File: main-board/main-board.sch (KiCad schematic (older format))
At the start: 112 parts, among them J1 BOOT, J10 8P8CDouble, J11 Qwiic, J12 Qwiic, J13 Qwiic, J14 YELLOW, J15 GREEN, J2 USB Header, J3 JTAG, J5 StatusPanel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

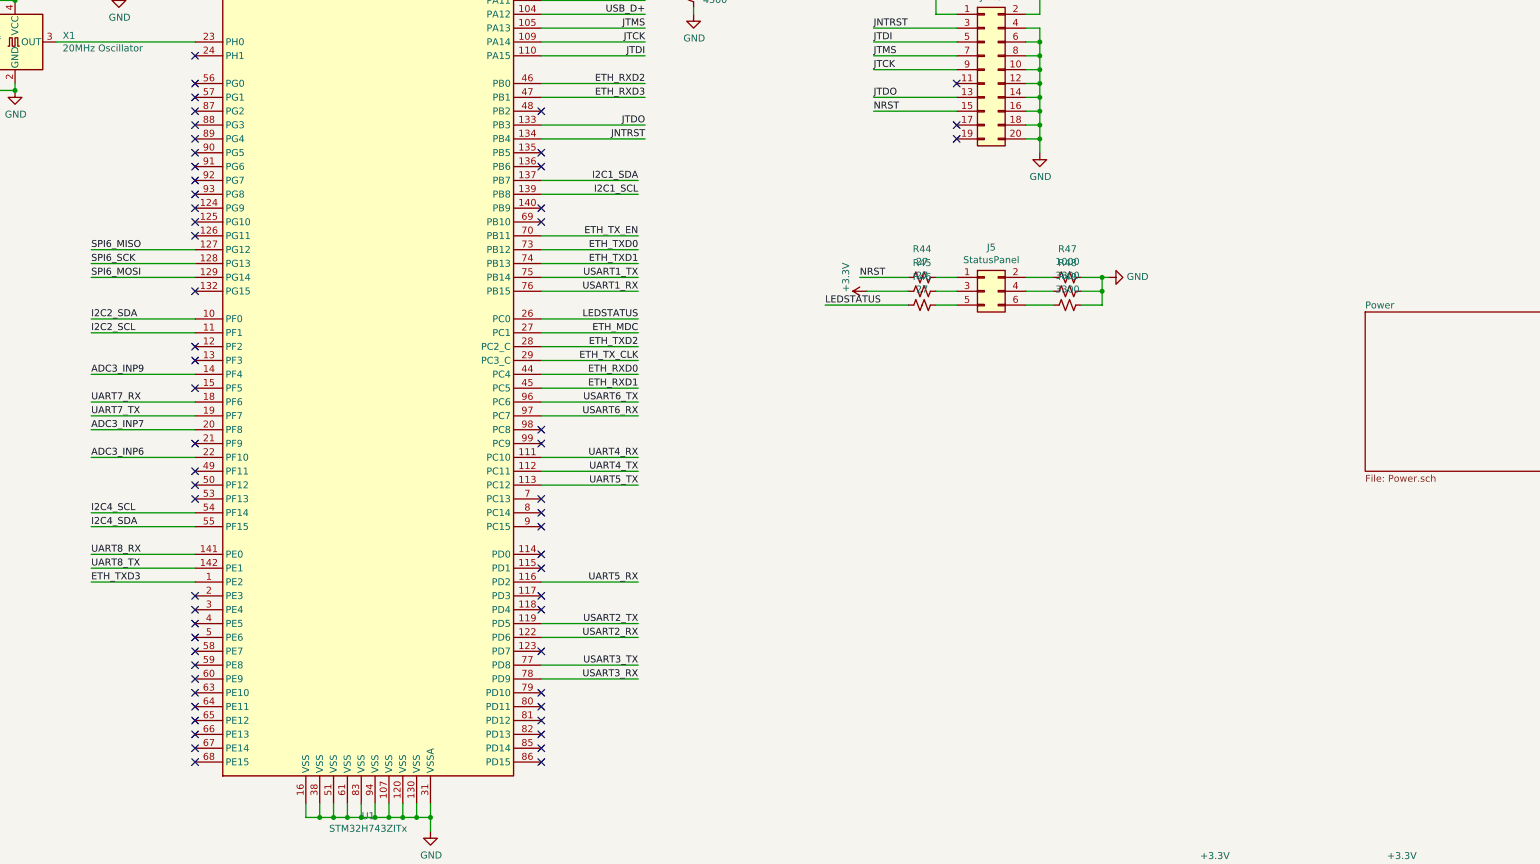
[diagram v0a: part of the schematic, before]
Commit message: GPIO control lines for the MOSFET array
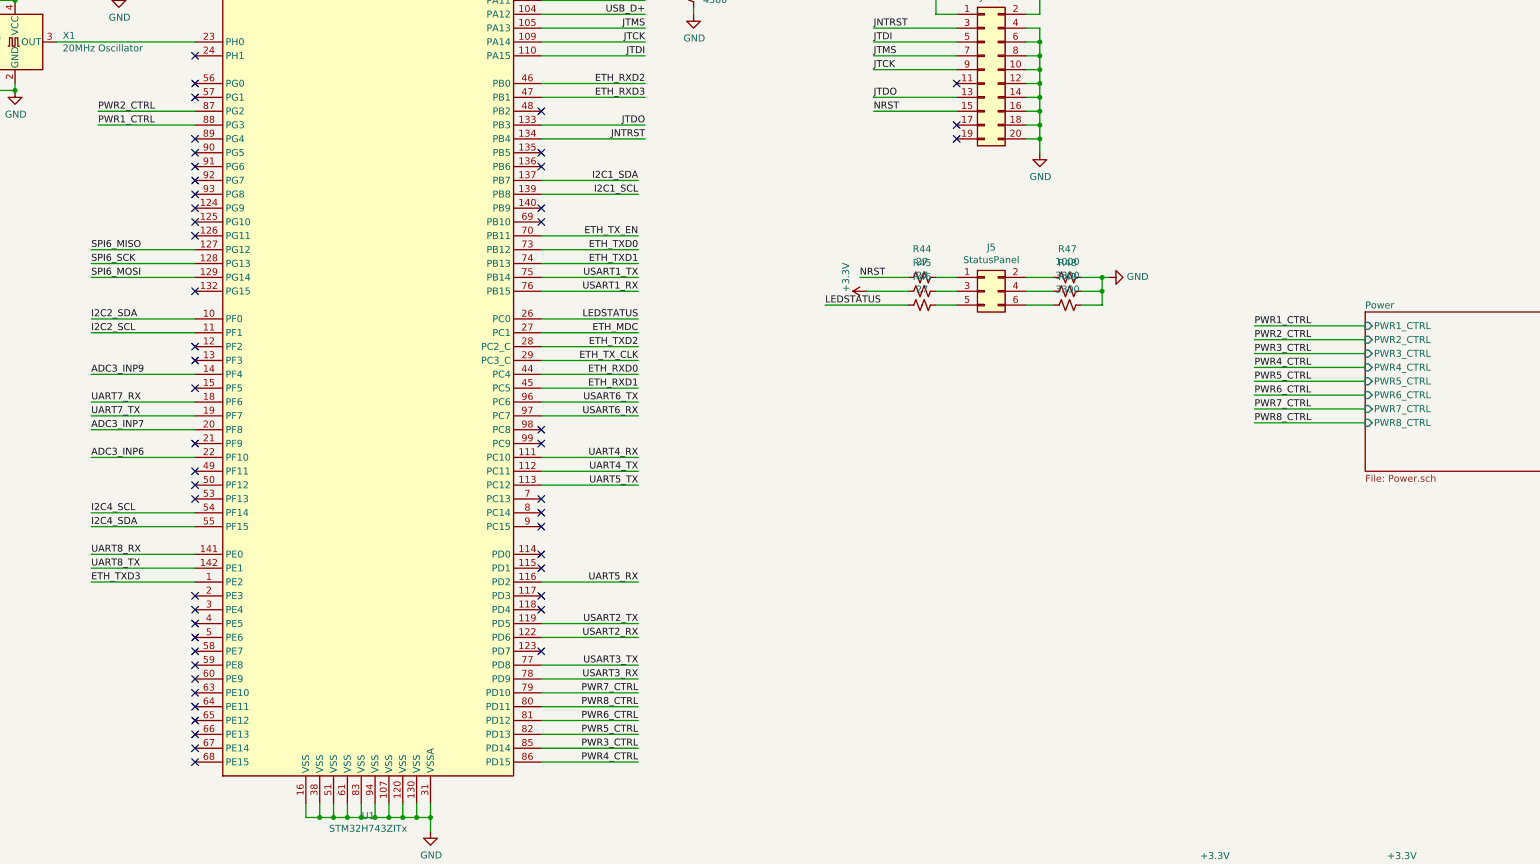
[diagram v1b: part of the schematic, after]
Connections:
- net PWR7_CTRL: now reaches U1.79 (PD10)
- net PWR8_CTRL: now reaches U1.80 (PD11)
- net PWR6_CTRL: now reaches U1.81 (PD12)
- net PWR5_CTRL: now reaches U1.82 (PD13)
- net PWR3_CTRL: now reaches U1.85 (PD14)
- net PWR4_CTRL: now reaches U1.86 (PD15)
- net PWR2_CTRL: now reaches U1.87 (PG2)
- net PWR1_CTRL: now reaches U1.88 (PG3)
- no-connect marks 66 -> 58
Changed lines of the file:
@@
 	2300 9450 2500 9450
 NoConn ~ 2500 9350
-NoConn ~ 13150 9700
-NoConn ~ 13150 9600
-NoConn ~ 13150 9500
-NoConn ~ 13150 9400
-NoConn ~ 13150 9300
-NoConn ~ 13150 9200
 NoConn ~ 13150 8900
 NoConn ~ 13150 7800
@@
 NoConn ~ 10650 5300
 NoConn ~ 10650 5200
-NoConn ~ 10650 5100
 NoConn ~ 10650 4800
 NoConn ~ 10650 4900
-NoConn ~ 10650 5000
 NoConn ~ 13150 3500
 NoConn ~ 13150 4100
@@
 F0 "Power" 50
 F1 "Power.sch" 50
+F2 "PWR1_CTRL" I L 19100 6550 50
+F3 "PWR3_CTRL" I L 19100 6750 50
+F4 "PWR2_CTRL" I L 19100 6650 50
+F5 "PWR4_CTRL" I L 19100 6850 50
+F6 "PWR6_CTRL" I L 19100 7050 50
+F7 "PWR5_CTRL" I L 19100 6950 50
+F8 "PWR7_CTRL" I L 19100 7150 50
+F9 "PWR8_CTRL" I L 19100 7250 50
 $EndSheet
 Connection ~ 9800 11250
@@
 Wire Wire Line
 	1050 2500 1300 2500
+Wire Wire Line
+	13150 9200 13850 9200
+Wire Wire Line
+	13150 9300 13850 9300
+Wire Wire Line
+	13150 9400 13850 9400
+Wire Wire Line
+	13150 9500 13850 9500
+Wire Wire Line
+	13150 9600 13850 9600
+Wire Wire Line
+	13150 9700 13850 9700
+Wire Wire Line
+	10650 5000 9950 5000
+Wire Wire Line
+	10650 5100 9950 5100
+Text Label 9950 5000 0    50   ~ 0
+PWR2_CTRL
+Text Label 9950 5100 0    50   ~ 0
+PWR1_CTRL
+Wire Wire Line
+	19100 6550 18300 6550
+Wire Wire Line
+	19100 6650 18300 6650
+Wire Wire Line
+	19100 6750 18300 6750
+Wire Wire Line
+	19100 6850 18300 6850
+Wire Wire Line
+	19100 6950 18300 6950
+Wire Wire Line
+	19100 7050 18300 7050
+Wire Wire Line
+	19100 7150 18300 7150
+Wire Wire Line
+	19100 7250 18300 7250
+Text Label 18300 6550 0    50   ~ 0
+PWR1_CTRL
+Text Label 18300 6650 0    50   ~ 0
+PWR2_CTRL
+Text Label 18300 6750 0    50   ~ 0
+PWR3_CTRL
+Text Label 18300 6850 0    50   ~ 0
+PWR4_CTRL
+Text Label 18300 6950 0    50   ~ 0
+PWR5_CTRL
+Text Label 18300 7050 0    50   ~ 0
+PWR6_CTRL
+Text Label 18300 7150 0    50   ~ 0
+PWR7_CTRL
+Text Label 18300 7250 0    50   ~ 0
+PWR8_CTRL
+Text Label 13850 9700 2    50   ~ 0
+PWR4_CTRL
+Text Label 13850 9600 2    50   ~ 0
+PWR3_CTRL
+Text Label 13850 9500 2    50   ~ 0
+PWR5_CTRL
+Text Label 13850 9400 2    50   ~ 0
+PWR6_CTRL
+Text Label 13850 9300 2    50   ~ 0
+PWR8_CTRL
+Text Label 13850 9200 2    50   ~ 0
+PWR7_CTRL
 $EndSCHEMATC

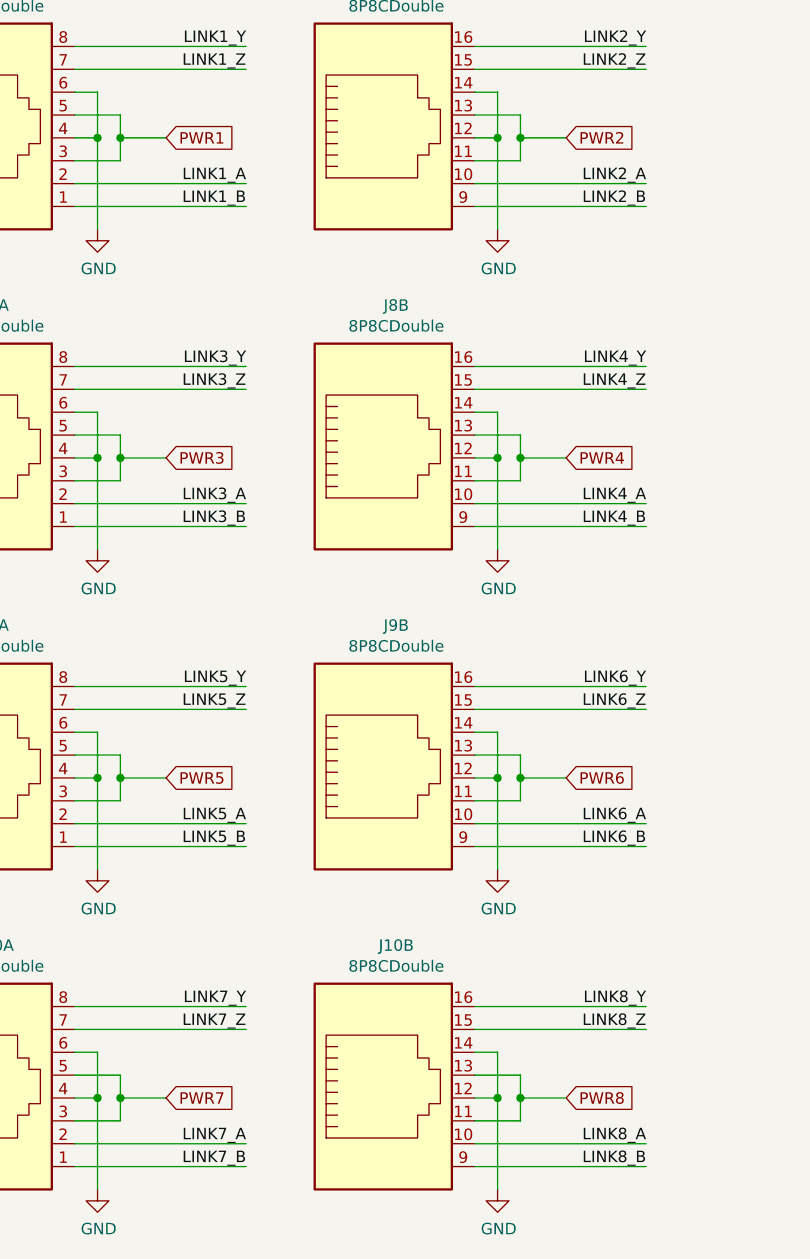
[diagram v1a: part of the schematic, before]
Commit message: Correct RS485 Z/Y pin swap
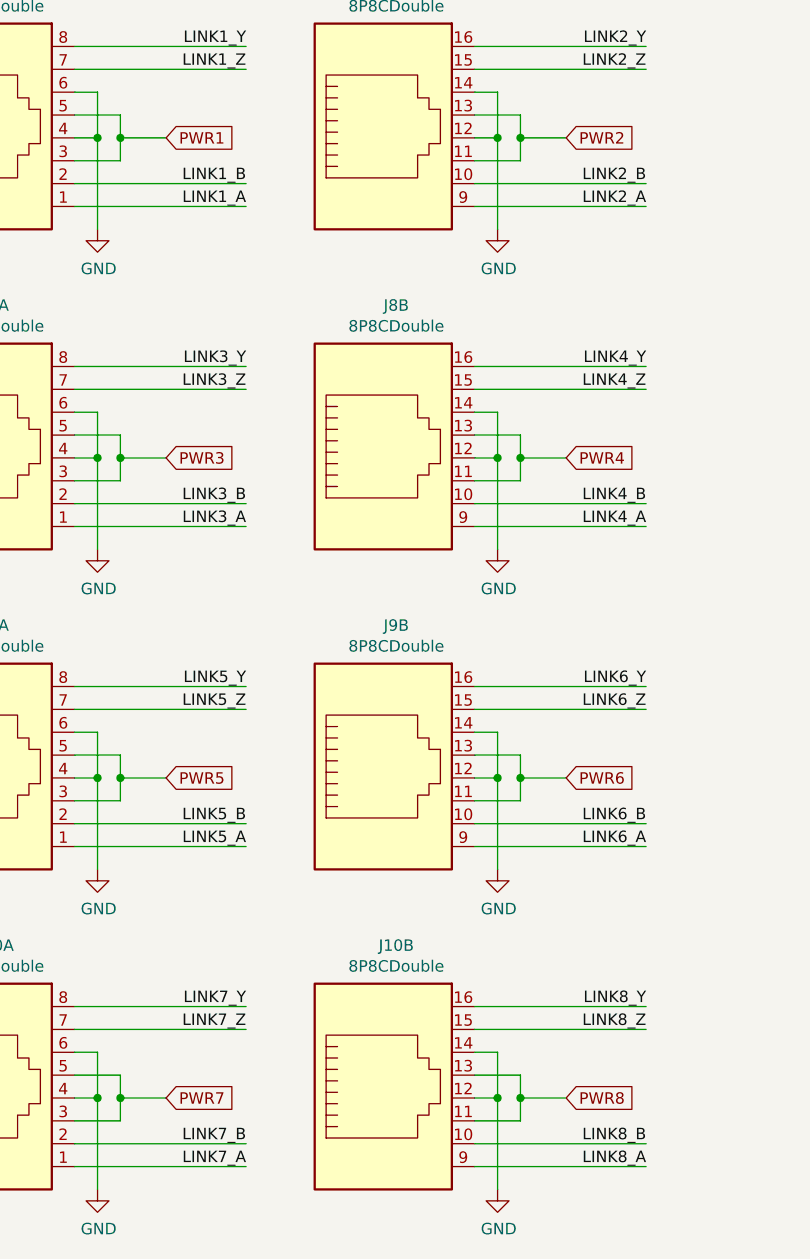
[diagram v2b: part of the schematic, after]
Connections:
- net LINK1_A: now also J7.1; no longer J7.2
- net LINK1_B: now also J7.2; no longer J7.1
- net LINK2_A: now also J7.9; no longer J7.10
- net LINK2_B: now also J7.10; no longer J7.9
- net LINK3_A: now also J8.1; no longer J8.2
- net LINK3_B: now also J8.2; no longer J8.1
- net LINK4_A: now also J8.9; no longer J8.10
- net LINK4_B: now also J8.10; no longer J8.9
- net LINK5_A: now also J9.1; no longer J9.2
- net LINK5_B: now also J9.2; no longer J9.1
- net LINK6_A: now also J9.9; no longer J9.10
- net LINK6_B: now also J9.10; no longer J9.9
- net LINK7_A: now also J10.1; no longer J10.2
- net LINK7_B: now also J10.2; no longer J10.1
- net LINK8_A: now also J10.9; no longer J10.10
- net LINK8_B: now also J10.10; no longer J10.9
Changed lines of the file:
@@
 LINK1_Z
 Text Label 10350 11450 2    50   ~ 0
+LINK1_B
+Text Label 10350 11550 2    50   ~ 0
 LINK1_A
-Text Label 10350 11550 2    50   ~ 0
-LINK1_B
 Text Label 12100 10850 2    50   ~ 0
 LINK2_Y
@@
 LINK2_Z
 Text Label 12100 11450 2    50   ~ 0
+LINK2_B
+Text Label 12100 11550 2    50   ~ 0
 LINK2_A
-Text Label 12100 11550 2    50   ~ 0
-LINK2_B
 Wire Wire Line
 	10650 8000 9900 8000
@@
 LINK3_Z
 Text Label 10350 12850 2    50   ~ 0
+LINK3_B
+Text Label 10350 12950 2    50   ~ 0
 LINK3_A
-Text Label 10350 12950 2    50   ~ 0
-LINK3_B
 Text Label 12100 12250 2    50   ~ 0
 LINK4_Y
@@
 LINK4_Z
 Text Label 12100 12850 2    50   ~ 0
+LINK4_B
+Text Label 12100 12950 2    50   ~ 0
 LINK4_A
-Text Label 12100 12950 2    50   ~ 0
-LINK4_B
 Text Label 10350 13650 2    50   ~ 0
 LINK5_Y
@@
 LINK5_Z
 Text Label 10350 14250 2    50   ~ 0
+LINK5_B
+Text Label 10350 14350 2    50   ~ 0
 LINK5_A
-Text Label 10350 14350 2    50   ~ 0
-LINK5_B
 Text Label 10350 15050 2    50   ~ 0
 LINK7_Y
@@
 LINK7_Z
 Text Label 10350 15650 2    50   ~ 0
+LINK7_B
+Text Label 10350 15750 2    50   ~ 0
 LINK7_A
-Text Label 10350 15750 2    50   ~ 0
-LINK7_B
 Text Label 12100 13650 2    50   ~ 0
 LINK6_Y
@@
 LINK6_Z
 Text Label 12100 14250 2    50   ~ 0
+LINK6_B
+Text Label 12100 14350 2    50   ~ 0
 LINK6_A
-Text Label 12100 14350 2    50   ~ 0
-LINK6_B
 Text Label 12100 15050 2    50   ~ 0
 LINK8_Y
@@
 LINK8_Z
 Text Label 12100 15650 2    50   ~ 0
+LINK8_B
+Text Label 12100 15750 2    50   ~ 0
 LINK8_A
-Text Label 12100 15750 2    50   ~ 0
-LINK8_B
 $Comp
 L Device:Ferrite_Bead_Small FB6

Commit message: Fix UART and I2C pin errors. Add ETH INTRP and RXER pins.
Various vias added, and passives packed in better around the ethernet.
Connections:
- net I2C1_SCL: now also U1.136 (PB6); no longer U1.139 (PB8)
- net UART4_RX: now also U1.112 (PC11); no longer U1.111 (PC10)
- net UART4_TX: now also U1.111 (PC10); no longer U1.112 (PC11)
- net ETH_RXER: now reaches U1.41 (PA5)
- net ETH_RXER: now also U4.29 (RXER/ISO)
- net ETH_INTRP: now reaches U1.42 (PA6)
- net ETH_INTRP: now also U4.32 (INTRP)
- no-connect marks 58 -> 54
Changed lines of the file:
@@
 UART5_TX
 Text Label 13850 7600 2    50   ~ 0
-UART4_TX
-Text Label 13850 7500 2    50   ~ 0
 UART4_RX
+Text Label 13850 7500 2    50   ~ 0
+UART4_TX
 Wire Wire Line
 	13150 4400 13900 4400
@@
 ETH_RX_DV
 NoConn ~ 2500 6500
-NoConn ~ 2500 7300
 $Comp
 L Device:R_Small_US R7
@@
 Wire Wire Line
 	2300 9450 2500 9450
-NoConn ~ 2500 9350
 NoConn ~ 13150 8900
 NoConn ~ 13150 7800
@@
 NoConn ~ 13150 5000
 NoConn ~ 13150 5300
-NoConn ~ 13150 5400
 NoConn ~ 13150 5700
 NoConn ~ 13150 7300
@@
 	1250 6300 1600 6300
 Wire Wire Line
-	13150 5600 13850 5600
+	13150 5400 13850 5400
 Wire Wire Line
 	13150 5500 13850 5500
 Text Label 13850 5500 2    50   ~ 0
 I2C1_SDA
-Text Label 13850 5600 2    50   ~ 0
+Text Label 13850 5400 2    50   ~ 0
 I2C1_SCL
 Wire Wire Line
@@
 Text GLabel 10000 15450 2    50   Input ~ 0
 PWR7
-NoConn ~ 13150 3700
-NoConn ~ 13150 3600
 Wire Wire Line
 	10650 6100 9900 6100
@@
 Text Label 13850 9200 2    50   ~ 0
 PWR7_CTRL
+NoConn ~ 13150 5600
+Wire Wire Line
+	2500 7300 2000 7300
+Text Label 2000 7300 0    50   ~ 0
+ETH_RXER
+Wire Wire Line
+	13150 3700 13900 3700
+Text Label 13900 3700 2    50   ~ 0
+ETH_INTRP
+Wire Wire Line
+	13150 3600 13900 3600
+Text Label 13900 3600 2    50   ~ 0
+ETH_RXER
+Wire Wire Line
+	2500 9350 2000 9350
+Text Label 2000 9350 0    50   ~ 0
+ETH_INTRP
 $EndSCHEMATC

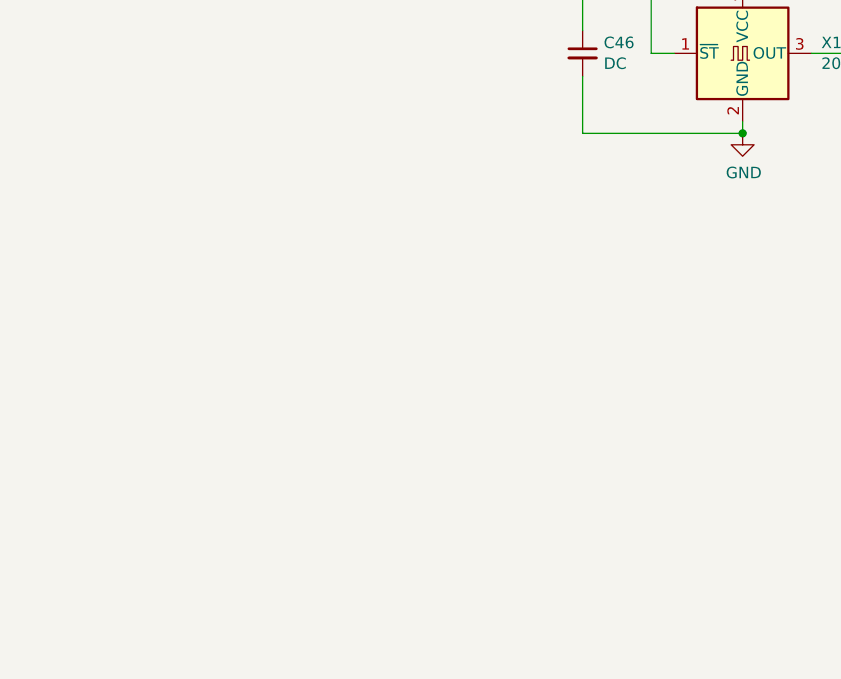
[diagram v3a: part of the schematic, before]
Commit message: Include a SPI flash
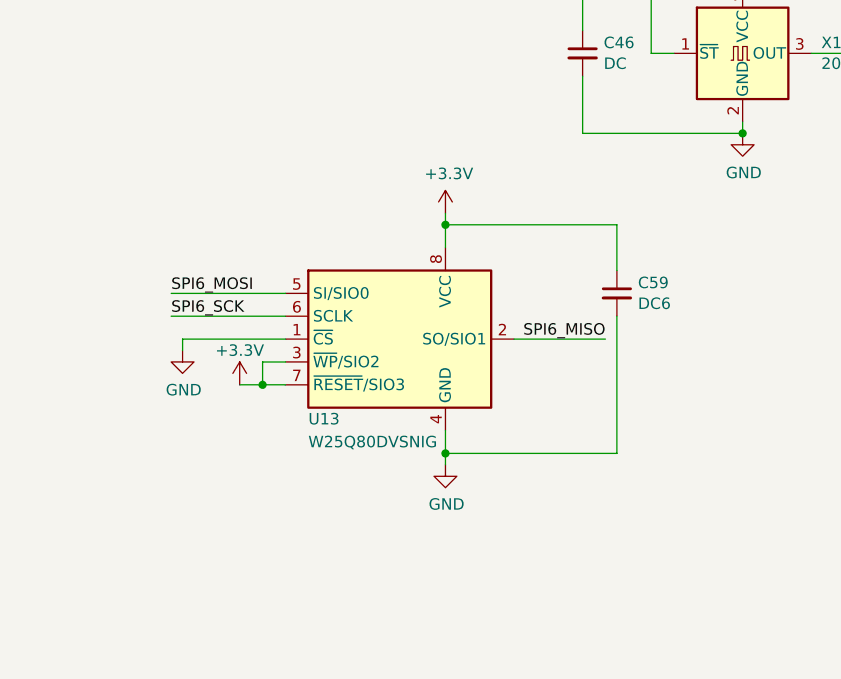
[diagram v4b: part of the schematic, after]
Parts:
- added C59: DC6, Capacitors_SMD:C_0805, symbol Device:C_Small
- added U13: W25Q80DVSNIG, Housings_SOIC:SOIC-8_3.9x4.9mm_Pitch1.27mm, symbol Memory_Flash:MX25R3235FM1xx0
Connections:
- net +3V3: now also C59.1, U13.3 (~WP~/SIO2), U13.7 (~RESET~/SIO3), U13.8 (VCC)
- net GND: now also C59.2, U13.1 (~CS), U13.4 (GND)
- net SPI6_MISO: now also U13.2 (SO/SIO1)
- net SPI6_MOSI: now also U13.5 (SI/SIO0)
- net SPI6_SCK: now also U13.6 (SCLK)
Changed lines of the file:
@@
 Text Label 2000 9350 0    50   ~ 0
 ETH_INTRP
+$Comp
+L Memory_Flash:MX25R3235FM1xx0 U13
+U 1 1 6096229F
+P 7850 5750
+F 0 "U13" H 7450 5400 50  0000 L CNN
+F 1 "W25Q80DVSNIG" H 7450 5300 50  0000 L CNN
+F 2 "Housings_SOIC:SOIC-8_3.9x4.9mm_Pitch1.27mm" H 7850 5150 50  0001 C CNN
+F 3 "http://www.macronix.com/Lists/Datasheet/Attachments/7534/MX25R3235F,%20Wide%20Range,%2032Mb,%20v1.6.pdf" H 7850 5750 50  0001 C CNN
+	1    7850 5750
+	1    0    0    -1
+$EndComp
+$Comp
+L Device:C_Small C59
+U 1 1 6096423A
+P 8800 5550
+F 0 "C59" H 8892 5596 50  0000 L CNN
+F 1 "DC6" H 8892 5505 50  0000 L CNN
+F 2 "Capacitors_SMD:C_0805" H 8800 5550 50  0001 C CNN
+F 3 "~" H 8800 5550 50  0001 C CNN
+	1    8800 5550
+	1    0    0    -1
+$EndComp
+Wire Wire Line
+	8050 5350 8050 5250
+Wire Wire Line
+	8050 5250 8800 5250
+Wire Wire Line
+	8800 5250 8800 5450
+Wire Wire Line
+	8050 6150 8050 6250
+Wire Wire Line
+	8050 6250 8800 6250
+Wire Wire Line
+	8800 6250 8800 5650
+Wire Wire Line
+	8050 5250 8050 5200
+Connection ~ 8050 5250
+Wire Wire Line
+	8050 6250 8050 6300
+Connection ~ 8050 6250
+$Comp
+L power:GND #PWR0191
+U 1 1 60C0E178
+P 8050 6300
+F 0 "#PWR0191" H 8050 6050 50  0001 C CNN
+F 1 "GND" H 8055 6127 50  0000 C CNN
+F 2 "" H 8050 6300 50  0001 C CNN
+F 3 "" H 8050 6300 50  0001 C CNN
+	1    8050 6300
+	1    0    0    -1
+$EndComp
+$Comp
+L power:+3.3V #PWR0192
+U 1 1 60C0F35C
+P 8050 5200
+F 0 "#PWR0192" H 8050 5050 50  0001 C CNN
+F 1 "+3.3V" H 8065 5373 50  0000 C CNN
+F 2 "" H 8050 5200 50  0001 C CNN
+F 3 "" H 8050 5200 50  0001 C CNN
+	1    8050 5200
+	1    0    0    -1
+$EndComp
+Wire Wire Line
+	7350 5550 6850 5550
+Text Label 6850 5550 0    50   ~ 0
+SPI6_MOSI
+Wire Wire Line
+	7350 5650 6850 5650
+Text Label 6850 5650 0    50   ~ 0
+SPI6_SCK
+Wire Wire Line
+	8350 5750 8750 5750
+Text Label 8750 5750 2    50   ~ 0
+SPI6_MISO
+Wire Wire Line
+	7350 5850 7250 5850
+Wire Wire Line
+	7250 5850 7250 5950
+Wire Wire Line
+	7250 5950 7350 5950
+$Comp
+L power:+3.3V #PWR0193
+U 1 1 61387829
+P 7150 5950
+F 0 "#PWR0193" H 7150 5800 50  0001 C CNN
+F 1 "+3.3V" H 7150 6100 50  0000 C CNN
+F 2 "" H 7150 5950 50  0001 C CNN
+F 3 "" H 7150 5950 50  0001 C CNN
+	1    7150 5950
+	1    0    0    -1
+$EndComp
+Wire Wire Line
+	7150 5950 7250 5950
+Connection ~ 7250 5950
+Wire Wire Line
+	6900 5750 6900 5800
+Wire Wire Line
+	6900 5750 7350 5750
+$Comp
+L power:GND #PWR0194
+U 1 1 615968B2
+P 6900 5800
+F 0 "#PWR0194" H 6900 5550 50  0001 C CNN
+F 1 "GND" H 6905 5627 50  0000 C CNN
+F 2 "" H 6900 5800 50  0001 C CNN
+F 3 "" H 6900 5800 50  0001 C CNN
+	1    6900 5800
+	1    0    0    -1
+$EndComp
 $EndSCHEMATC
